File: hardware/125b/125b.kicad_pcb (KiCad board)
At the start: 2 copper layers, 59 x 75 mm, 52 parts, among them J1 Guitar in, J2 Barrel_Jack, J3 Conn_02x05_Odd_Even_MountingP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, J4 Guitar out, SW1 SW_DIP_x02, SW2 RotaryEncoder_Switch, SW3 Switch 1, SW4 Switch 2, U1 L78L05_TO92, U2 TL074

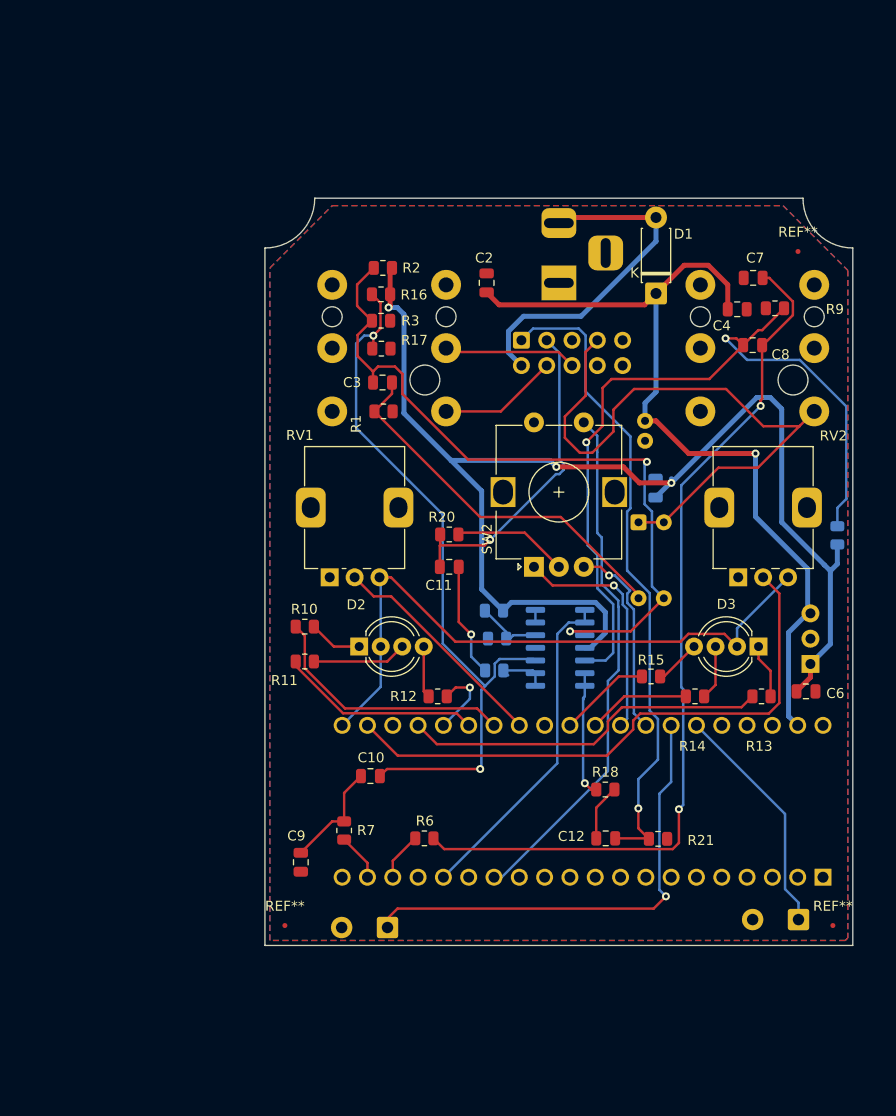
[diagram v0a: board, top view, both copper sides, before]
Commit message: get new stereo sockets on schematic and pcb
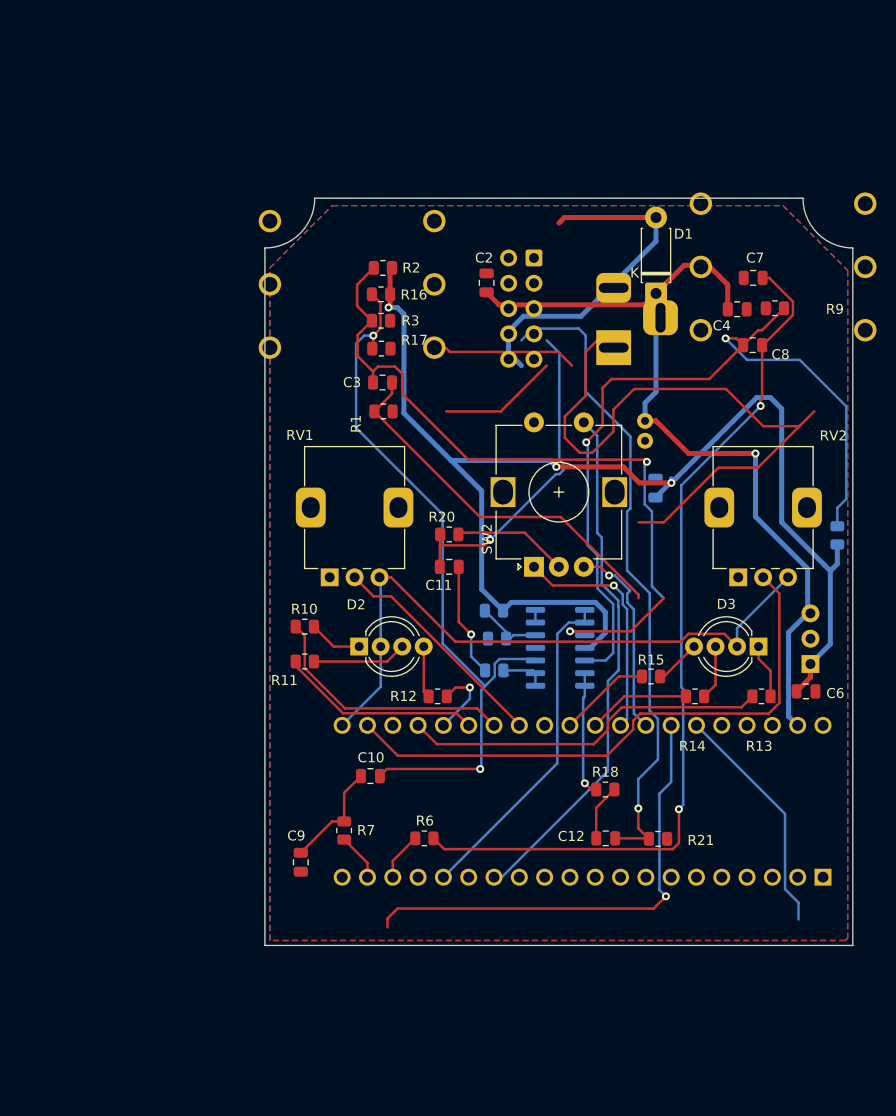
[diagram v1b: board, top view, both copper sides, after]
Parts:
- removed REF** (x3): Fiducial_0.5mm_Mask2mm, Fiducial:Fiducial_0.5mm_Mask2mm
- removed SW1: SW_DIP_x02, Button_Switch_THT:SW_DIP_SPSTx02_Slide_9.78x7.26mm_W7.62mm_P2.54mm
- removed SW3: Switch 1, Connector_Wire:SolderWire-0.5sqmm_1x02_P4.6mm_D0.9mm_OD2.1mm
- removed SW4: Switch 2, Connector_Wire:SolderWire-0.5sqmm_1x02_P4.6mm_D0.9mm_OD2.1mm
- J1, J4: footprint Project:Jack_6.35mm_Neutrik_NRJ6HF-1-AU_Horizontal -> Project:NYS215
- moved J4 18.8 mm to (98.5, 50.0)
- moved J1 14.0 mm to (141.8, 48.2)
- moved J2 8.51 mm to (133.0, 50.0)
- moved J3 8.36 mm to (125.0, 41.0), turned to 180 degrees
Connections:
- A1 pad 34: Net-(A1-SAI2_FS) -> /fsw8
- A1 pad 35: Net-(A1-SAI2_SCK) -> /fsw10
- J3 pad 10: unconnected-(J3-Pin_10-Pad10) -> /fsw10
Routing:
- net GND: track 11.6 -> 74.7 mm
- net /fsw7: track 63.1 -> 0.00 mm
- net Net-(A1-SAI2_FS): track 47.7 -> 0.00 mm, vias 1 -> 0
- net /fsw8: track 0.00 -> 47.7 mm, vias 0 -> 1
- net Net-(A1-SAI2_SCK): track 23.7 -> 0.00 mm
- net /fsw10: track 0.00 -> 23.7 mm
- net /fsw4: track 12.0 -> 25.4 mm
- net /fsw6: track 13.4 -> 0.00 mm

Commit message: Wire connectors for push switches and add slide spdt
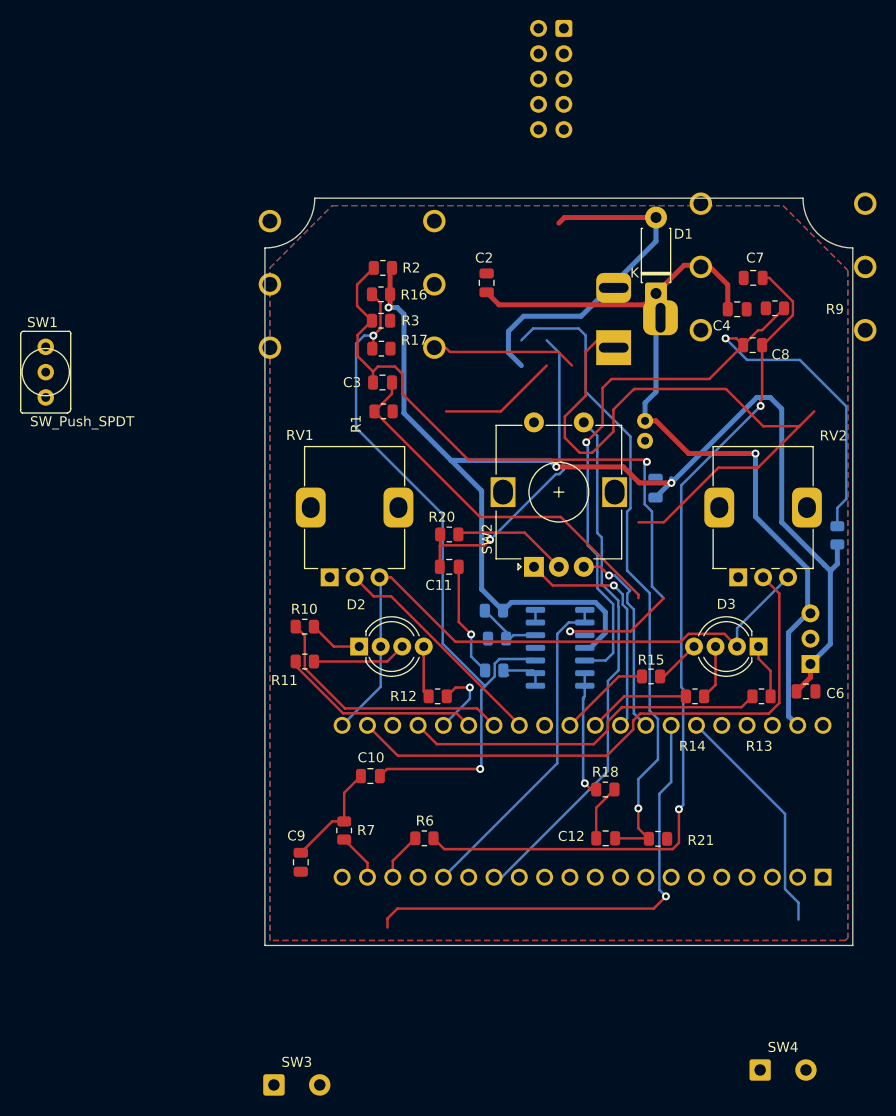
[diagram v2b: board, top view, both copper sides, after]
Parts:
- added SW1: SW_Push_SPDT, PCM_4ms_Switch:Switch_Toggle_SPDT_SubMini, F.Cu at (76.0, 52.5)
- added SW3: SW_Push, Connector_Wire:SolderWire-0.5sqmm_1x02_P4.6mm_D0.9mm_OD2.1mm, F.Cu at (98.9, 124.0)
- added SW4: SW_Push, Connector_Wire:SolderWire-0.5sqmm_1x02_P4.6mm_D0.9mm_OD2.1mm, F.Cu at (147.7, 122.5)
- moved J3 23.2 mm to (128.0, 18.0)

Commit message: Retraced and various parts moved and adjusted
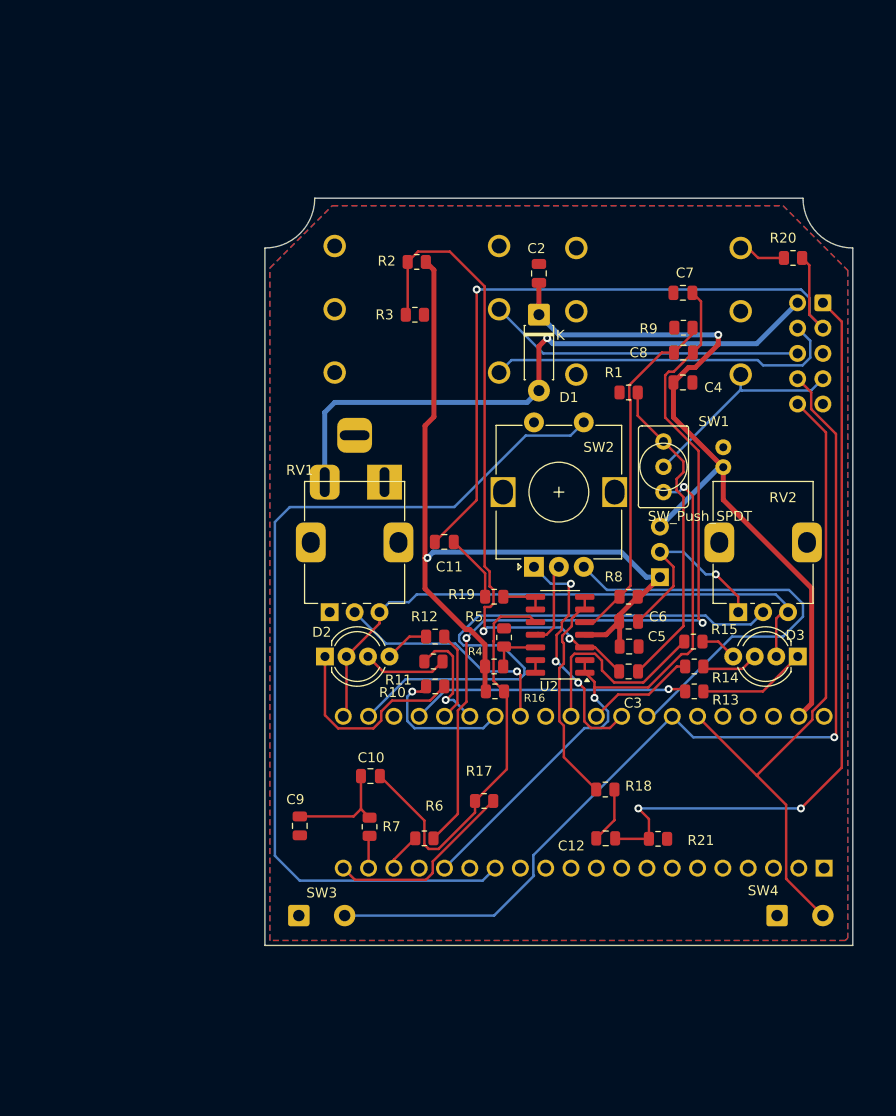
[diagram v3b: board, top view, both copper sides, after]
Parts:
- C5, R19, R4, R5, R8, U2: moved to F.Cu
- moved SW1 62.7 mm to (138.0, 62.0)
- moved R17 46.6 mm to (120.0, 95.5)
- moved R20 44.3 mm to (151.0, 41.0), turned to 180 degrees
- moved R16 41.5 mm to (121.1, 84.5), turned to 0 degrees
- moved C3 38.1 mm to (134.5, 82.5)
- moved J3 37.9 mm to (154.0, 45.5)
- moved J2 26.7 mm to (110.0, 63.5), turned to 0 degrees
- moved R1 24.7 mm to (134.5, 54.5), turned to 180 degrees
- moved R8 21.8 mm to (134.5, 75.0), turned to 180 degrees
- moved C6 19.1 mm to (134.5, 77.5)
- moved U1 17.4 mm to (137.6, 73.0)
- moved SW3 17.2 mm to (101.4, 107.0)
- moved C5 16.1 mm to (134.6, 80.0), turned to 180 degrees
- moved SW4 15.6 mm to (149.4, 107.0)
- moved R10 14.4 mm to (115.1, 84.0)
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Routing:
- net /fsw8: track 47.7 -> 97.2 mm
- net Net-(U2B-+): track 82.5 -> 35.4 mm, vias 2 -> 0
- net +5V: track 131.1 -> 84.3 mm, vias 3 -> 1
- net /fsw10: track 23.7 -> 66.5 mm
- net /fsw3: track 32.5 -> 72.3 mm
- net /ENC_CLICK: track 52.7 -> 92.3 mm
- net Net-(U2C-+): track 73.8 -> 41.1 mm, vias 2 -> 0
- net /fsw6: track 0.00 -> 31.8 mm
- net /fsw2: track 34.9 -> 62.1 mm, vias 0 -> 1
- net /Left in: track 33.7 -> 60.0 mm, vias 0 -> 2
- net /ENC_B: track 20.0 -> 44.6 mm, vias 1 -> 0
- net GND: track 74.7 -> 53.1 mm, vias 0 -> 1
- net /fsw7: track 0.00 -> 21.2 mm
- net Net-(D2-RK): track 5.38 -> 20.7 mm
- net /LED_2_B: track 9.26 -> 20.9 mm
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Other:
- board text added: "Crouds v0.6 Denis Crowdy, Prog Pedals"
- board text removed: "Crouds v0.5 Denis Crowdy, Prog Pedals"
